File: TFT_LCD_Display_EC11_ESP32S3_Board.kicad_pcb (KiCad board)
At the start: 2 copper layers, 91 x 44 mm, 44 parts, among them J1 MOLEX-503398-1892, J2 USB_C_Receptacle_USB2.0_16P, J3 I2C, J4 POWER, J5 SPARE, J6 TFT-LCD-DISPLAY-EC11, SW1 BOOT, SW2 RESET, U1 MCP1826S, U2 ESP32-S3-WROOM-1

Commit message: r3.1 - Orientation D1 was wrong
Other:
- board text added: "Rev.3.1 [13-06-2026]"
- board text removed: "Rev.3.0 [06-06-2026]"
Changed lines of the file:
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@@
 	)
 	(paper "A4")
+	(title_block
+		(title "Piggy Back Board for TFT LCD Display EC11 witj ESP32-S3")
+		(date "2026-06-13")
+		(rev "Rev. 3.1")
+		(company "by Willem Aandewiel")
+	)
 	(layers
 		(0 "F.Cu" signal)
@@
 		(layer "F.SilkS")
 	)
-	(gr_line
-		(start 128 124.5)
-		(end 131.25 124.5)
+	(gr_circle
+		(center 124.8 84.8)
+		(end 125 84.8)
 		(stroke
 			(width 0.5)
 			(type solid)
 		)
+		(fill no)
 		(layer "F.SilkS")
 	)
-	(gr_circle
-		(center 132.5 88)
-		(end 132.7 88)
+	(gr_line
+		(start 128 124.5)
+		(end 131.25 124.5)
 		(stroke
 			(width 0.5)
 			(type solid)
 		)
-		(fill no)
 		(layer "F.SilkS")
 	)
@@
 		)
 	)
-	(gr_text "Rev.3.0 [06-06-2026]"
+	(gr_text "Rev.3.1 [13-06-2026]"
 		(at 151.5 82.5 180)
 		(layer "F.SilkS")
@@
 		)
 	)
-	(gr_text "Rev.3.0 [06-06-2026]"
+	(gr_text "Rev.3.1 [13-06-2026]"
 		(at 126 83 180)
 		(layer "B.SilkS")

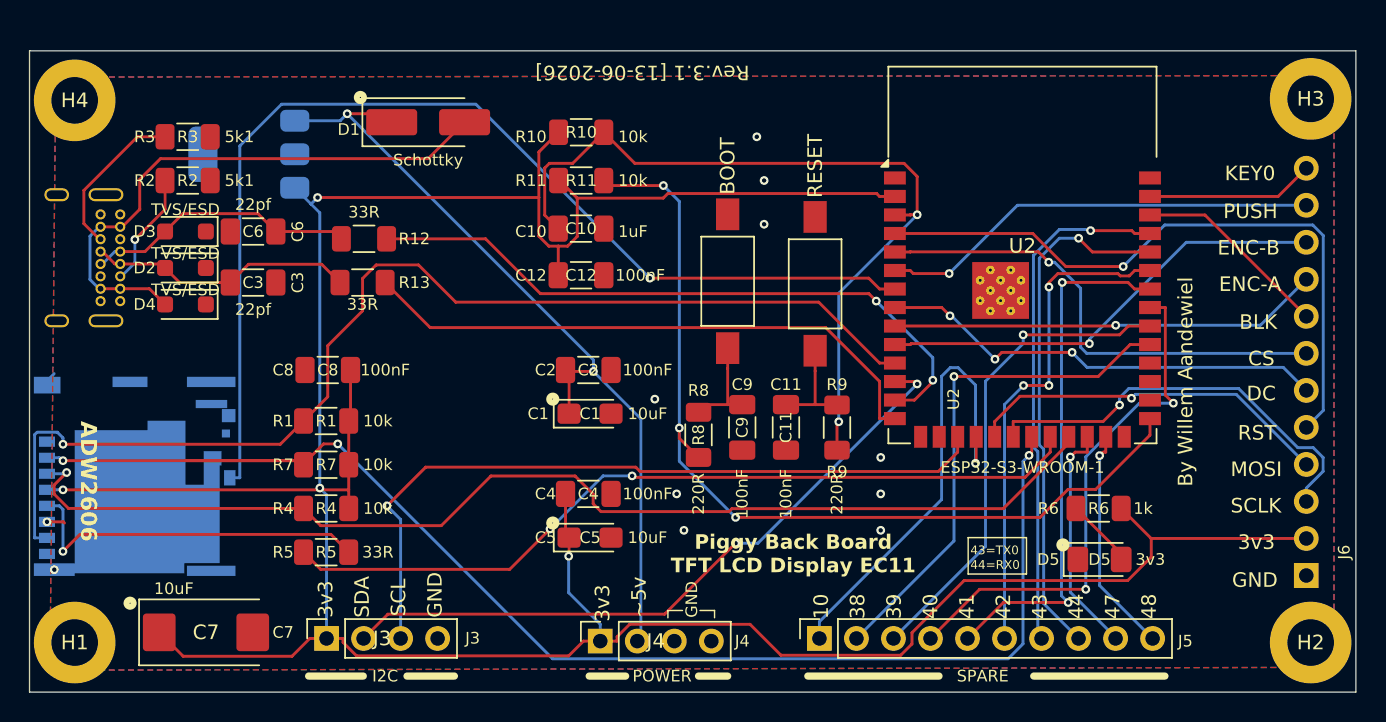
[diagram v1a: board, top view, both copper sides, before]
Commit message: J4 ~5v now is real VBUS 5v
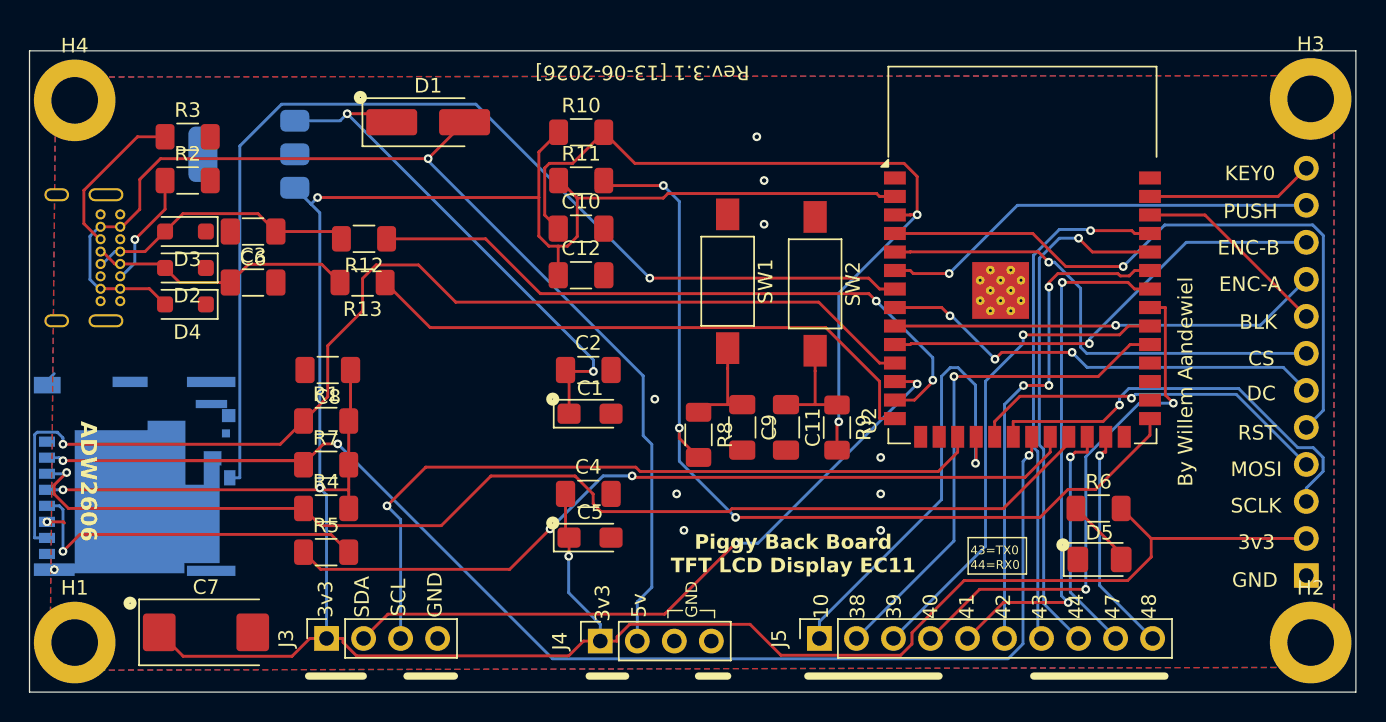
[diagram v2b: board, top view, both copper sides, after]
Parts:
- C1, C5: footprint localLib:CP_EIA-3216-18_Kemet-A_HandSolder -> Capacitor_Tantalum_SMD:CP_EIA-3216-18_Kemet-A_HandSolder
- C10, C11, C12, C2, C3, C4, C6, C8, C9: footprint localLib:C_1206_3216Metric_Pad1.33x1.80mm_HandSolder -> Capacitor_SMD:C_1206_3216Metric_Pad1.33x1.80mm_HandSolder
- C7: footprint localLib:CP_EIA-7343-31_Kemet-D_HandSolder -> Capacitor_Tantalum_SMD:CP_EIA-7343-31_Kemet-D_HandSolder
- D1: footprint localLib:D_SMA_Handsoldering -> Diode_SMD:D_SMA_Handsoldering
- D2, D3, D4: footprint localLib:D_SOD-123F -> Diode_SMD:D_SOD-123F
- D5: value 3v3 -> LED; footprint localLib:LED_1206_3216Metric_Pad1.42x1.75mm_HandSolder -> LED_SMD:LED_1206_3216Metric_Pad1.42x1.75mm_HandSolder
- H1, H2, H3, H4: footprint localLib:MountingHole_3.2mm_M3_DIN965_Pad -> MountingHole:MountingHole_3.2mm_M3_DIN965_Pad
- J1: footprint localLib:MOLEX_503398-1892_mod -> MyNewLibrary:MOLEX_503398-1892_mod
- J2: footprint localLib:USB_C_Receptacle_GCT_USB4085 -> Connector_USB:USB_C_Receptacle_GCT_USB4085
- J3, J4: footprint localLib:PinSocket_1x04_P2.54mm_Vertical -> Connector_PinSocket_2.54mm:PinSocket_1x04_P2.54mm_Vertical
- J5: footprint localLib:PinSocket_1x10_P2.54mm_Vertical -> Connector_PinSocket_2.54mm:PinSocket_1x10_P2.54mm_Vertical
- J6: footprint localLib:PinHeader_1x12_P2.54mm_Vertical -> Connector_PinHeader_2.54mm:PinHeader_1x12_P2.54mm_Vertical
- R1, R10, R11, R12, R13, R2, R3, R4, R5, R6, R7, R8, R9: footprint localLib:R_1206_3216Metric_Pad1.30x1.75mm_HandSolder -> Resistor_SMD:R_1206_3216Metric_Pad1.30x1.75mm_HandSolder
- SW1: footprint localLib:SW_SPST_FSMSM -> Button_Switch_SMD:SW_SPST_FSMSM
- SW2: value RESET -> EN; footprint localLib:SW_SPST_FSMSM -> Button_Switch_SMD:SW_SPST_FSMSM
- U1: footprint localLib:SOT-223-3_TabPin2 -> Package_TO_SOT_SMD:SOT-223-3_TabPin2
- U2: footprint localLib:ESP32-S3-WROOM-1 -> RF_Module:ESP32-S3-WROOM-1
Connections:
- C1 pad 1: ~5v -> Net-(D1-K)
- C2 pad 1: ~5v -> Net-(D1-K)
- D1 pad 1: ~5v -> Net-(D1-K)
- J4 pad 2: ~5v -> VBUS
- U1 pad 1: ~5v -> Net-(D1-K)
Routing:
- net ~5v: track 56.6 -> 0.00 mm, vias 2 -> 0
- net VBUS: track 39.0 -> 78.9 mm, vias 0 -> 1
- net Net-(D1-K): track 0.00 -> 36.6 mm, vias 0 -> 2
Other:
- board text added: "5v"
- board text removed: "~5v"
